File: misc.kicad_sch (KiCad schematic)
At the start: 53 parts, among them J10 Molex_KK_1x4_0470531000, J11 Molex_KK_1x4_0470531000, J9 Molex_KK_1x4_0470531000, Q10 MMBT3904LT1G, Q5 BSS138-7-F, Q6 BSS84AKW, Q7 BSS138-7-F, Q8 BSS138-7-F, Q9 MMBT3904LT1G, U24 ADT7476AARQZ, U25 74LVC1G157-Q100H_SOT457, U26 74LVC1G157-Q100H_SOT457, U27 NTS0102_TSSOP, U28 NTS0102_TSSOP, U29 NTS0102_TSSOP

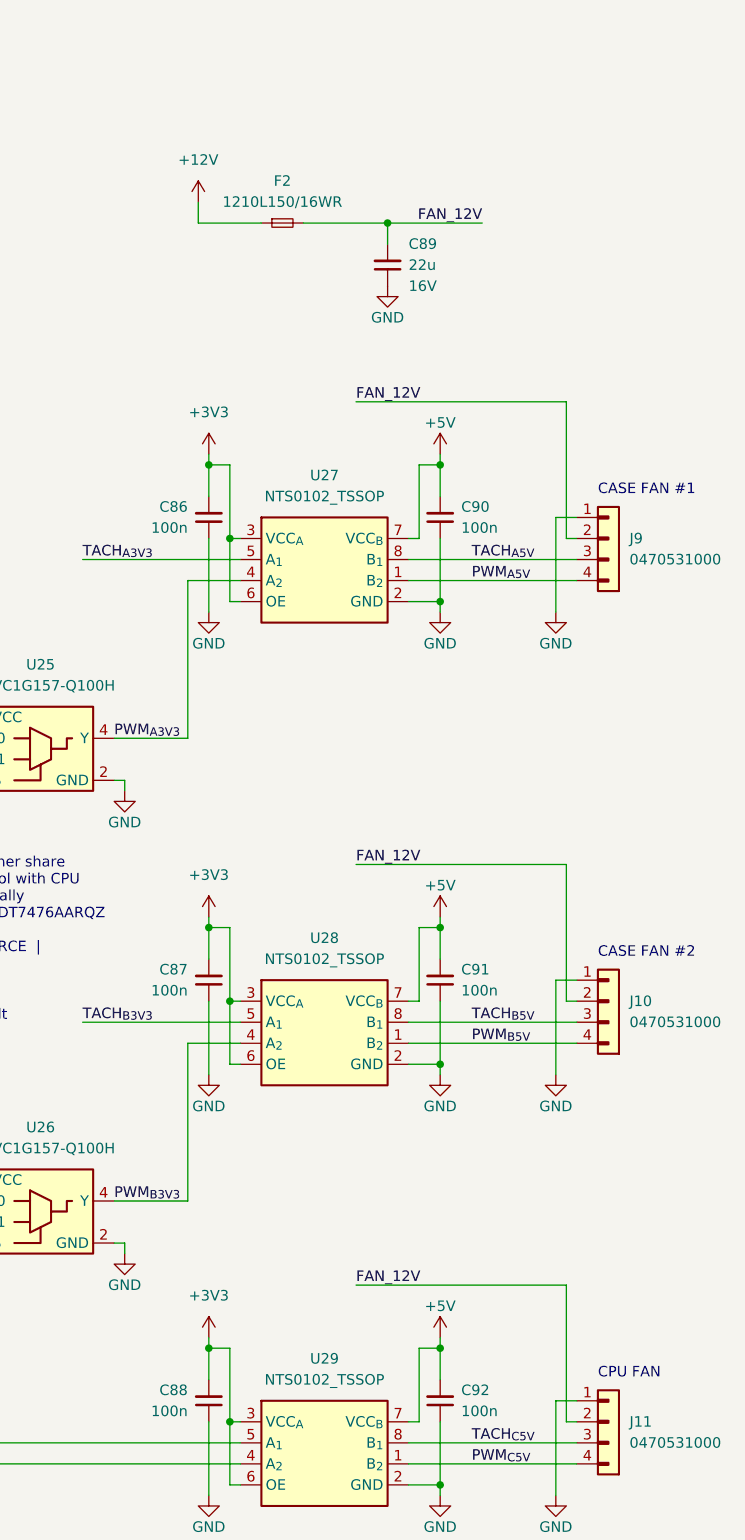
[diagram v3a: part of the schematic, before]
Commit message: [#58904] Change fan fuse and decoupling
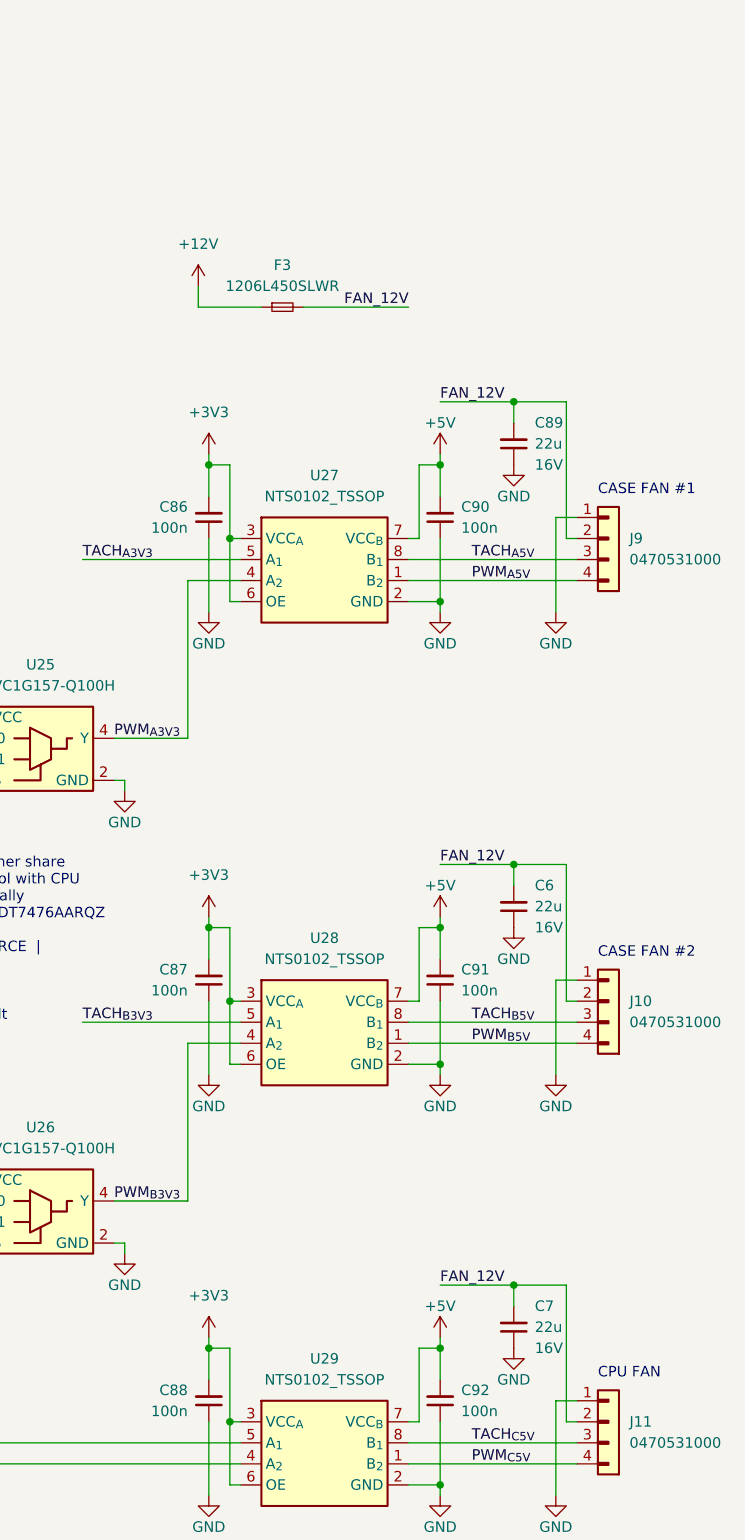
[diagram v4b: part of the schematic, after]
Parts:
- removed F2: PTC_3A_1210, antmicro-footprints:F_1210_3225Metric, symbol antmicroFuses:PTC_3A_1210
- added C6, C7: C_22u_16V_0603, antmicro-footprints:C_0603_1608Metric, symbol antmicroCapacitors0603:C_22u_16V_0603
- added F3: PTC_4.5A_1206, antmicro-footprints:F_1206_3216Metric, symbol antmicroFuses:PTC_4.5A_1206
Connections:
- net +12V: now also F3.1
- net FAN_12V: now also C6.2, C7.2, F3.2
- net GND: now also C6.1, C7.1
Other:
- moved on the sheet: C89

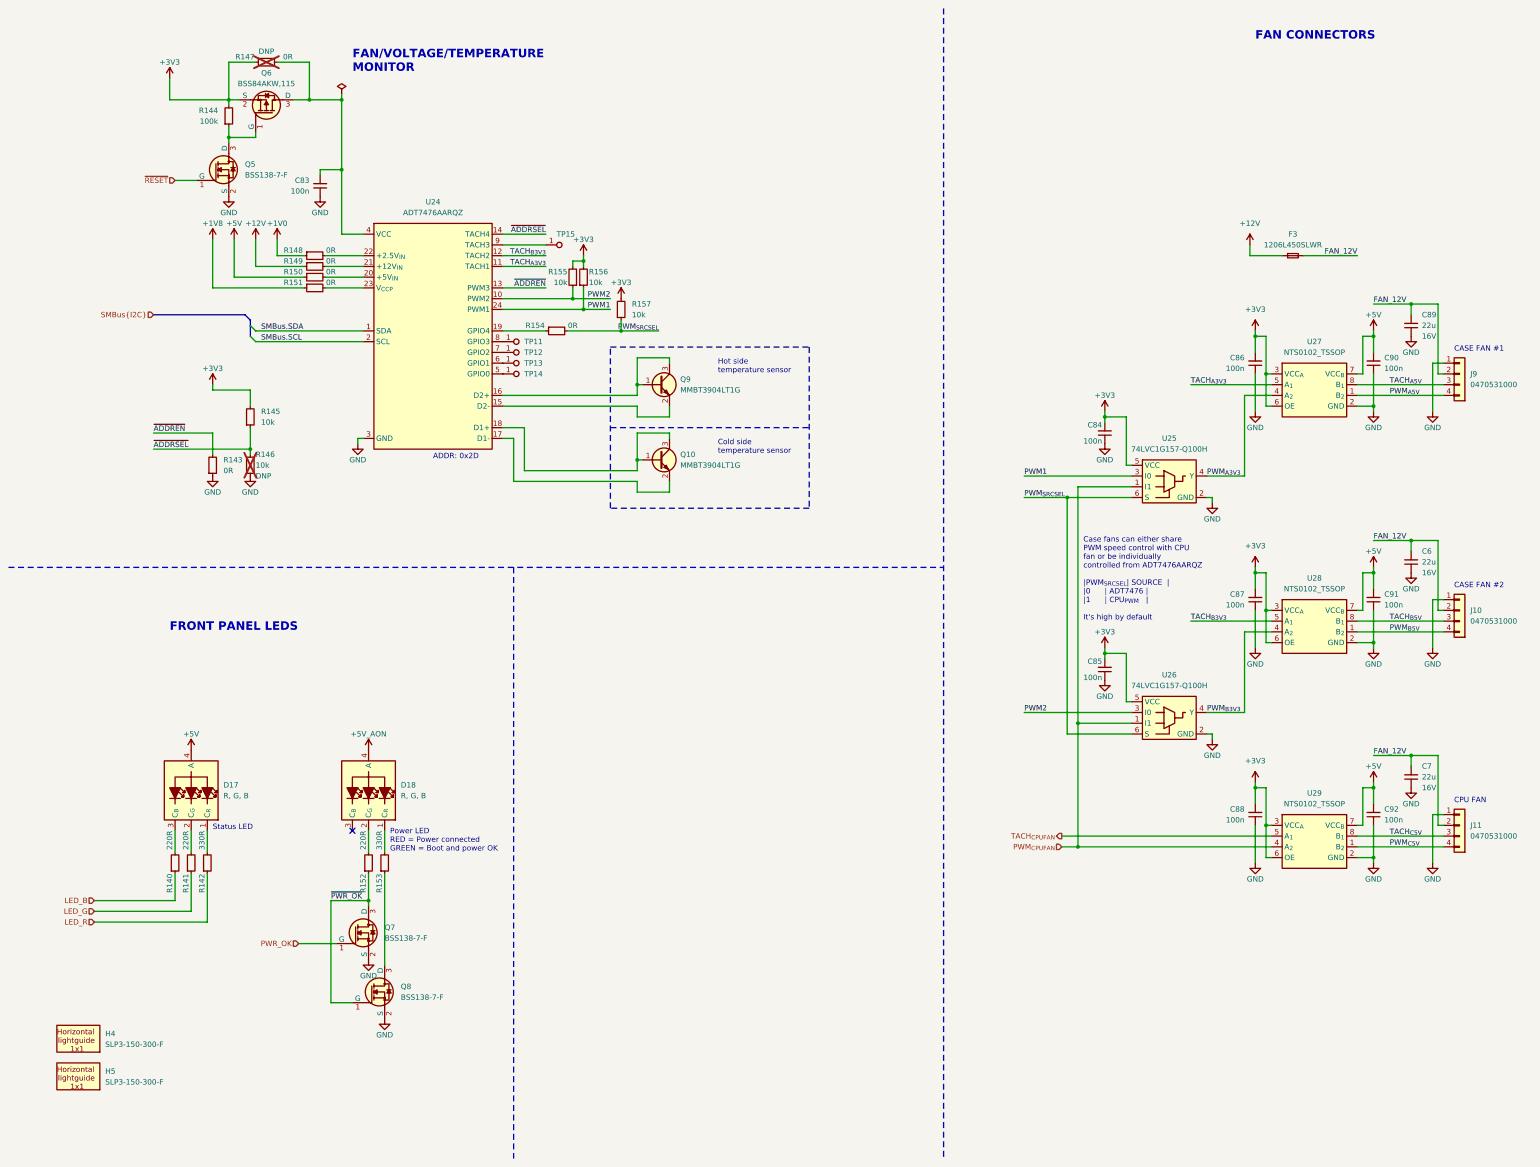
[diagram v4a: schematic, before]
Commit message: Update components from the library
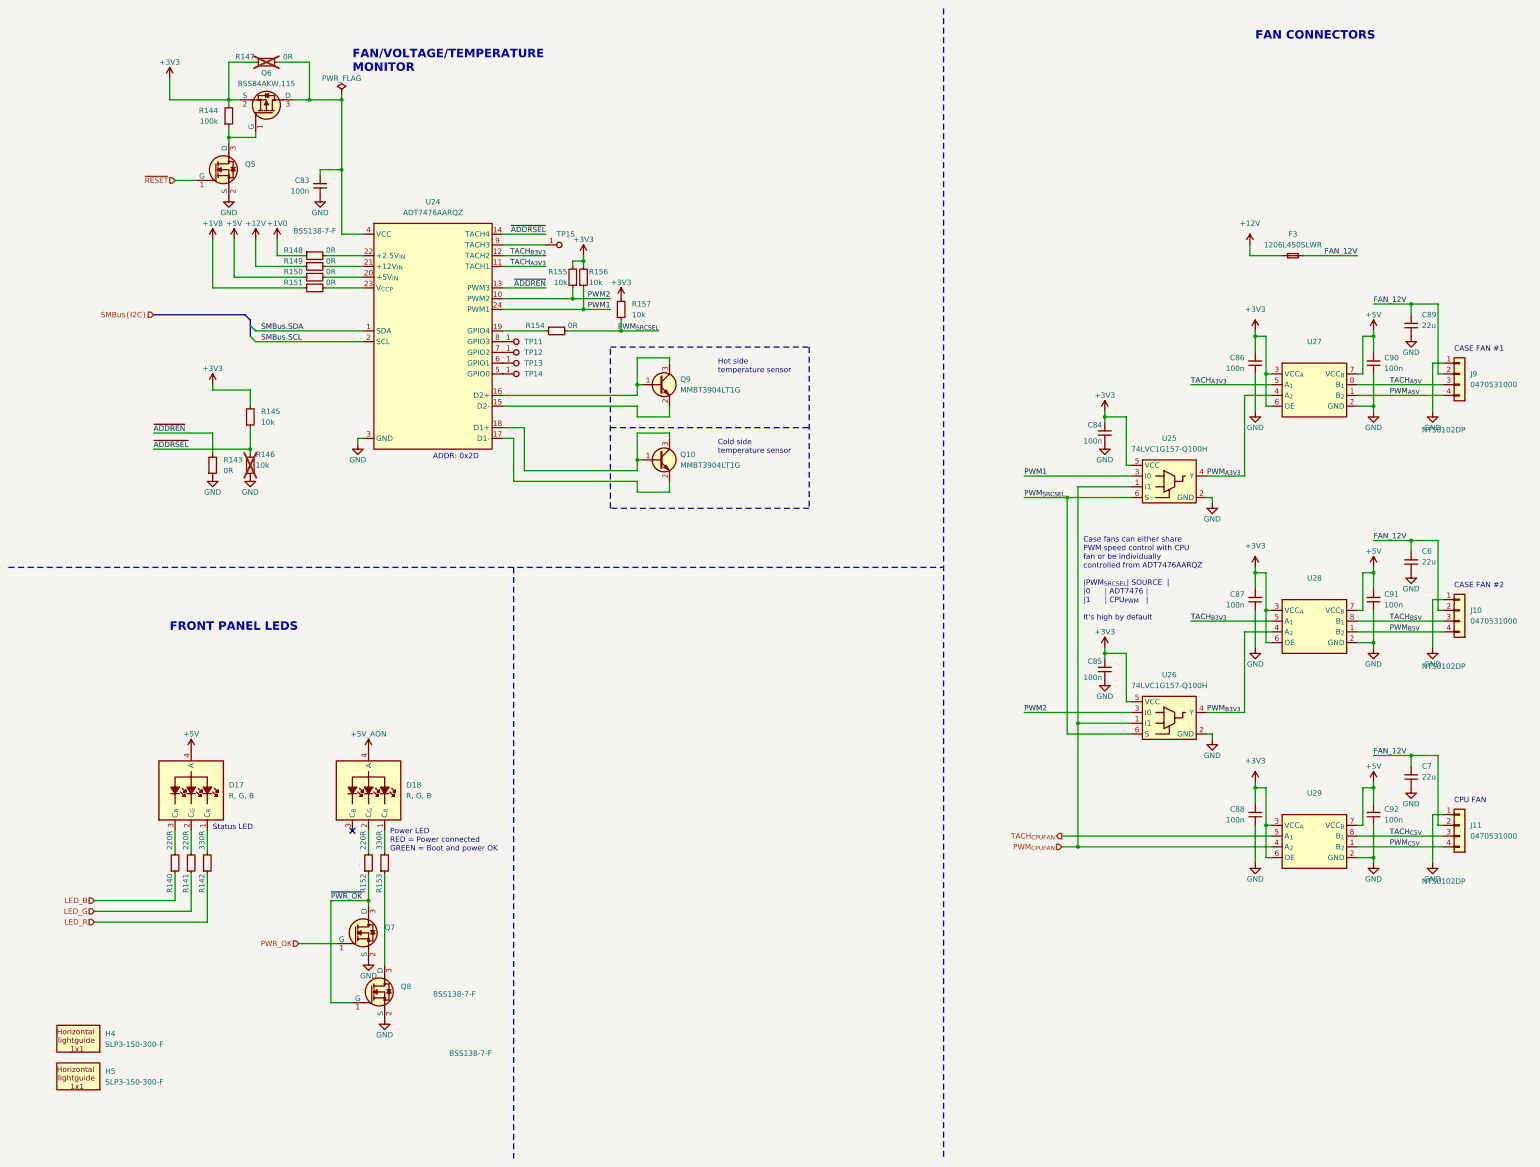
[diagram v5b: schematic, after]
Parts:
- C6, C7, C83, C84, C85, C86, C87, C88, C89, C90, C91, C92, Q10, Q9, R142, R143, R144, R145, R148, R149, R150, R151, R153, R154, R155, R156, R157, TP11, TP12, TP13, TP14, TP15: Public (none) -> False
- R140, R141, R152: Copyright Copyright (c) 2023 Antmicro -> (none); Public (none) -> False
- R146, R147: DNP DNP -> (none); Public (none) -> False
